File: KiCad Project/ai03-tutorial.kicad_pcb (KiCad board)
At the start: 2 copper layers, 76.5 x 38 mm, 24 parts, among them SW1 SW_Push, U1 ATmega32U4-A, Y1 16MHz

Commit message: Finished PCB guide part 5. Initial routing complete.
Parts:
- F1, SW1, USB1: moved to B.Cu
- moved C3 27.0 mm to (80.3, 79.9), turned to 0 degrees
- moved R1 23.6 mm to (81.7, 100.0), turned to 0 degrees
- moved R4 22.8 mm to (92.5, 79.9), turned to 180 degrees
- moved C1 22.8 mm to (84.4, 79.9), turned to 180 degrees
- moved C2 21.3 mm to (88.4, 79.9)
- moved C5 19.7 mm to (86.3, 100.0), turned to 180 degrees
- moved C4 19.3 mm to (91.2, 100.0), turned to 0 degrees
- moved C6 18.9 mm to (97.8, 86.2)
- moved C7 18.8 mm to (97.7, 95.0)
- moved Y1 16.4 mm to (97.7, 90.7), turned to 90 degrees
- moved U1 6.69 mm to (85.4, 90.3), turned to -90 degrees
- moved R3 4.65 mm to (70.3, 80.0), turned to -90 degrees
- moved F1 3.58 mm to (70.1, 89.8), turned to 0 degrees
- moved SW1 2.70 mm to (70.1, 97.8)
- moved R2 2.31 mm to (72.6, 80.0), turned to -90 degrees
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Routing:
- net GND: track 0.00 -> 142.1 mm
- net +5V: track 0.00 -> 88.8 mm
- net Net-(U1-~{RESET}): track 0.00 -> 33.8 mm
- net VCC: track 0.00 -> 32.3 mm
- net ROW0: track 0.00 -> 20.5 mm
- net ROW1: track 0.00 -> 20.2 mm
- net COL1: track 0.00 -> 19.0 mm
- net COL0: track 0.00 -> 19.0 mm
- net Net-(U1-D-): track 0.00 -> 14.9 mm
- net Net-(U1-D+): track 0.00 -> 13.8 mm
- net Net-(U1-XTAL1): track 0.00 -> 13.3 mm
- net Net-(U1-XTAL2): track 0.00 -> 10.3 mm
- net Net-(D3-A): track 0.00 -> 6.94 mm
- net Net-(D4-A): track 0.00 -> 6.89 mm
- net Net-(D1-A): track 0.00 -> 6.73 mm
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
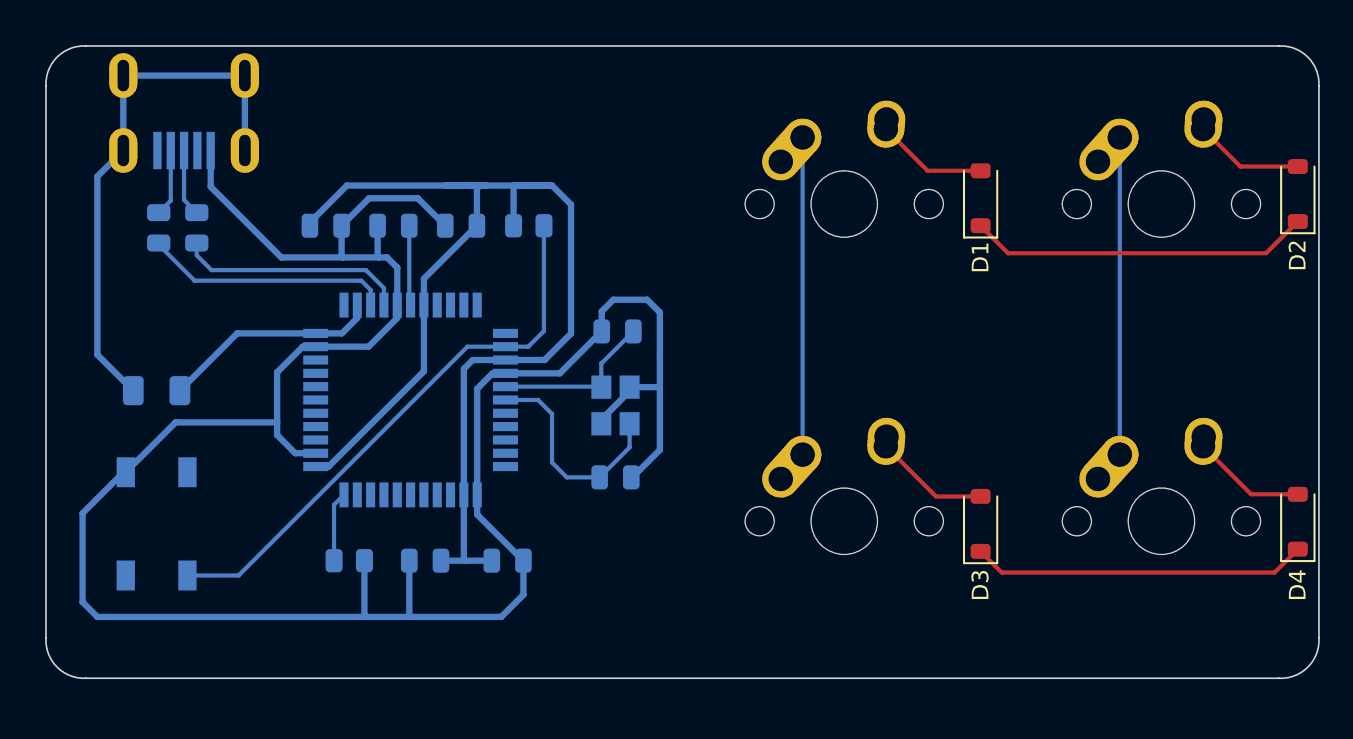
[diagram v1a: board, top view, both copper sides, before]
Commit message: Finished PCB guide part 6. Added ground copper layer.
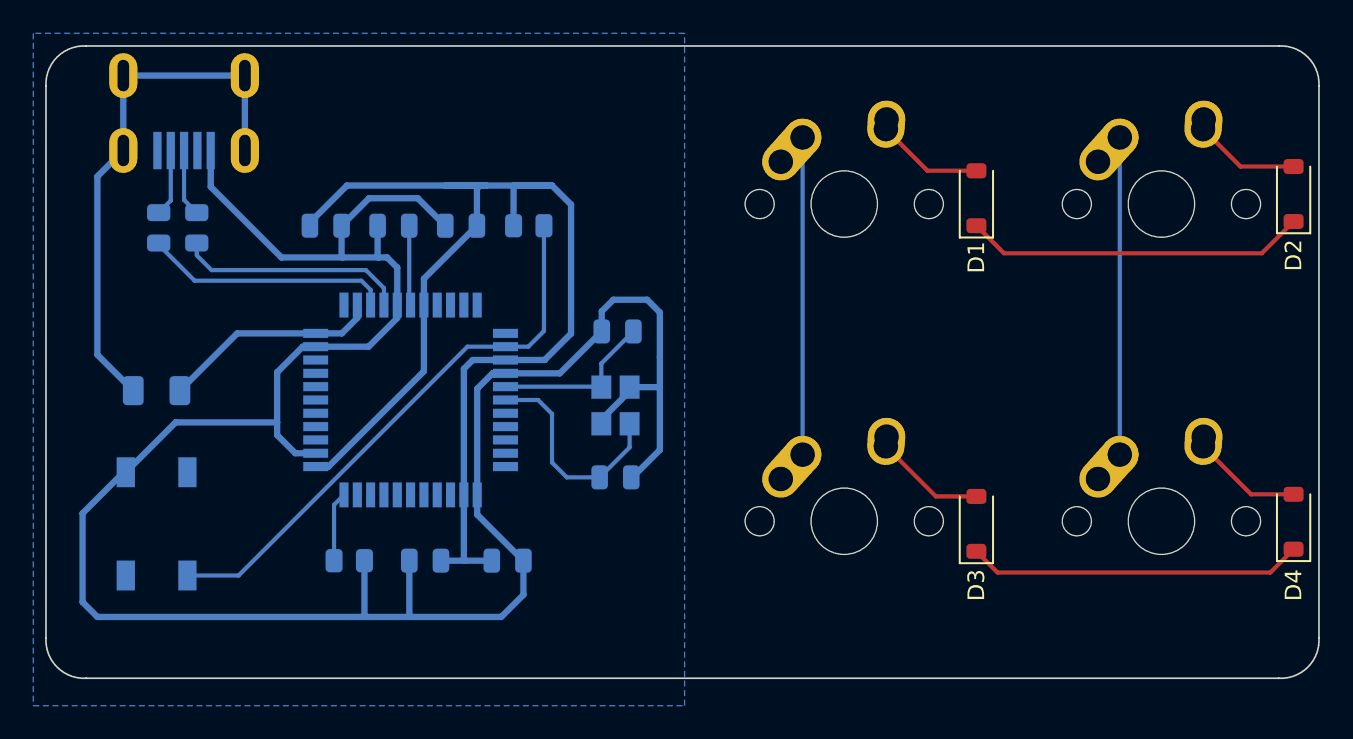
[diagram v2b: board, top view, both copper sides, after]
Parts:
- moved D1 0.25 mm to (119.4, 78.2)
- moved D3 0.25 mm to (119.4, 97.8)
- moved D2 0.25 mm to (138.4, 78.0)
- moved D4 0.25 mm to (138.4, 97.7)
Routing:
- added copper zone on B.Cu, net GND
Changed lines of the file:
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@@
   (net 48 "unconnected-(USB1-VBUS-Pad5)")
   (footprint "Diode_SMD:D_SOD-123" (layer "F.Cu")
-    (at 138.684 97.663 90)
+    (at 138.43 97.663 90)
     (descr "SOD-123")
     (tags "SOD-123")
@@
   )
   (footprint "Diode_SMD:D_SOD-123" (layer "F.Cu")
-    (at 138.684 77.978 90)
+    (at 138.43 77.978 90)
     (descr "SOD-123")
     (tags "SOD-123")
@@
   )
   (footprint "Diode_SMD:D_SOD-123" (layer "F.Cu")
-    (at 119.634 78.232 90)
+    (at 119.38 78.232 90)
     (descr "SOD-123")
     (tags "SOD-123")
@@
   )
   (footprint "Diode_SMD:D_SOD-123" (layer "F.Cu")
-    (at 119.634 97.79 90)
+    (at 119.38 97.79 90)
     (descr "SOD-123")
     (tags "SOD-123")
@@
   (segment (start 94.781 94.996) (end 96.752 94.996) (width 0.254) (layer "B.Cu") (net 5))
   (segment (start 93.892 94.107) (end 94.781 94.996) (width 0.254) (layer "B.Cu") (net 5))
-  (segment (start 121.286 81.534) (end 136.778 81.534) (width 0.254) (layer "F.Cu") (net 6))
-  (segment (start 136.778 81.534) (end 138.684 79.628) (width 0.254) (layer "F.Cu") (net 6))
-  (segment (start 119.634 79.882) (end 121.286 81.534) (width 0.254) (layer "F.Cu") (net 6))
-  (segment (start 116.44325 76.582) (end 119.634 76.582) (width 0.25) (layer "F.Cu") (net 7))
+  (segment (start 121.032 81.534) (end 136.524 81.534) (width 0.254) (layer "F.Cu") (net 6))
+  (segment (start 119.38 79.882) (end 121.032 81.534) (width 0.254) (layer "F.Cu") (net 6))
+  (segment (start 136.524 81.534) (end 138.43 79.628) (width 0.254) (layer "F.Cu") (net 6))
+  (segment (start 116.44325 76.582) (end 119.38 76.582) (width 0.25) (layer "F.Cu") (net 7))
   (segment (start 113.9425 74.08125) (end 116.44325 76.582) (width 0.25) (layer "F.Cu") (net 7))
+  (segment (start 135.23925 76.328) (end 138.43 76.328) (width 0.254) (layer "F.Cu") (net 8))
   (segment (start 132.9925 74.08125) (end 135.23925 76.328) (width 0.254) (layer "F.Cu") (net 8))
-  (segment (start 135.23925 76.328) (end 138.684 76.328) (width 0.254) (layer "F.Cu") (net 8))
-  (segment (start 119.634 99.44) (end 120.905 100.711) (width 0.254) (layer "F.Cu") (net 9))
-  (segment (start 137.286 100.711) (end 138.684 99.313) (width 0.254) (layer "F.Cu") (net 9))
-  (segment (start 120.905 100.711) (end 137.286 100.711) (width 0.254) (layer "F.Cu") (net 9))
-  (segment (start 116.95125 96.14) (end 119.634 96.14) (width 0.254) (layer "F.Cu") (net 10))
+  (segment (start 137.032 100.711) (end 138.43 99.313) (width 0.254) (layer "F.Cu") (net 9))
+  (segment (start 119.38 99.44) (end 120.651 100.711) (width 0.254) (layer "F.Cu") (net 9))
+  (segment (start 120.651 100.711) (end 137.032 100.711) (width 0.254) (layer "F.Cu") (net 9))
+  (segment (start 116.95125 96.14) (end 119.38 96.14) (width 0.254) (layer "F.Cu") (net 10))
   (segment (start 113.9425 93.13125) (end 116.95125 96.14) (width 0.254) (layer "F.Cu") (net 10))
-  (segment (start 135.87425 96.013) (end 138.684 96.013) (width 0.254) (layer "F.Cu") (net 11))
+  (segment (start 135.87425 96.013) (end 138.43 96.013) (width 0.254) (layer "F.Cu") (net 11))
   (segment (start 132.9925 93.13125) (end 135.87425 96.013) (width 0.254) (layer "F.Cu") (net 11))
   (segment (start 68.144 75.366) (end 66.587 76.923) (width 0.381) (layer "B.Cu") (net 12))
@@
   (segment (start 75.06855 100.89) (end 71.993 100.89) (width 0.254) (layer "B.Cu") (net 20))
   (segment (start 91.098 87.148) (end 88.81055 87.148) (width 0.254) (layer "B.Cu") (net 20))
+  (zone (net 2) (net_name "GND") (layer "B.Cu") (hatch edge 0.5)
+    (connect_pads (clearance 0.5))
+    (min_thickness 0.25) (filled_areas_thickness no)
+    (fill yes (thermal_gap 0.5) (thermal_bridge_width 0.5))
+    (polygon
+      (pts
+        (xy 62.738 108.712)
+        (xy 101.854 108.712)
+        (xy 101.854 68.326)
+        (xy 62.738 68.326)
+      )
+    )
+  )
 )

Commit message: Added matrix connections.
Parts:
- D1, D2, D3, D4: moved to B.Cu
- moved D1 19.2 mm to (138.5, 78.2)
- moved D3 19.2 mm to (138.5, 97.8)
- moved D2 19.0 mm to (119.5, 78.0)
- moved D4 19.0 mm to (119.5, 97.7)
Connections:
- U1 pad 18: unconnected-(U1-PD0-Pad18) -> ROW0
- U1 pad 19: unconnected-(U1-PD1-Pad19) -> COL0
- U1 pad 20: unconnected-(U1-PD2-Pad20) -> ROW1
- U1 pad 21: unconnected-(U1-PD3-Pad21) -> COL1
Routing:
- net COL1: track 19.0 -> 65.3 mm, vias 0 -> 1
- net ROW0: track 20.5 -> 59.0 mm
- net ROW1: track 20.2 -> 53.2 mm
- net Net-(D3-A): track 6.68 -> 28.7 mm
- net Net-(D1-A): track 6.47 -> 27.6 mm
- net COL0: track 19.0 -> 40.0 mm
- net Net-(D4-A): track 6.63 -> 15.6 mm
- net Net-(D2-A): track 6.37 -> 15.4 mm
